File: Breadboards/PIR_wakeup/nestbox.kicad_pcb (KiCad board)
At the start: 2 copper layers, 42.8 x 27.5 mm, 13 parts, among them P1 PINOUT

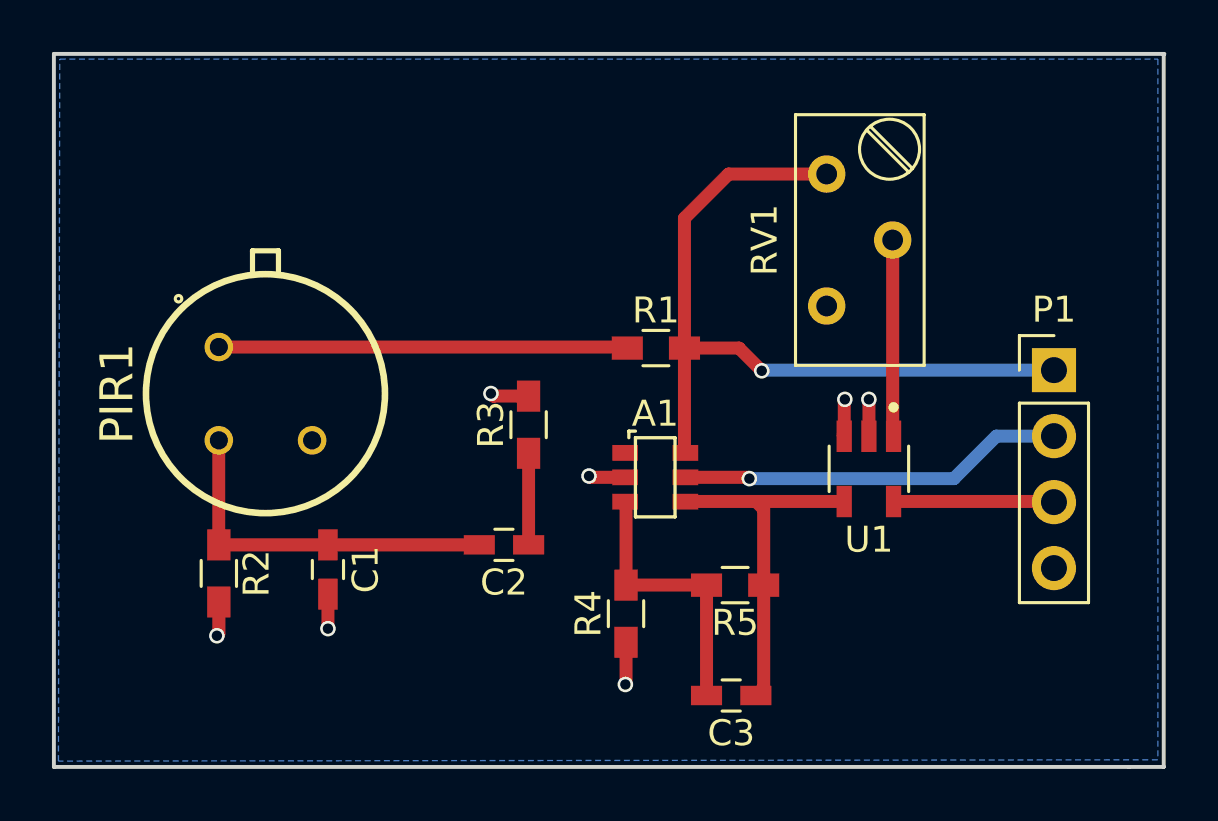
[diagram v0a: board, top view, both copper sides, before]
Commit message: Updated version of PCB
-Added component values on silk
- Added output pin connections on silk
- Cleaned silk and made it consistent trough all components
- Changed vias width to comply to manufacturer specifications
- Added missing trace
- Added decoupling capacitor on power input
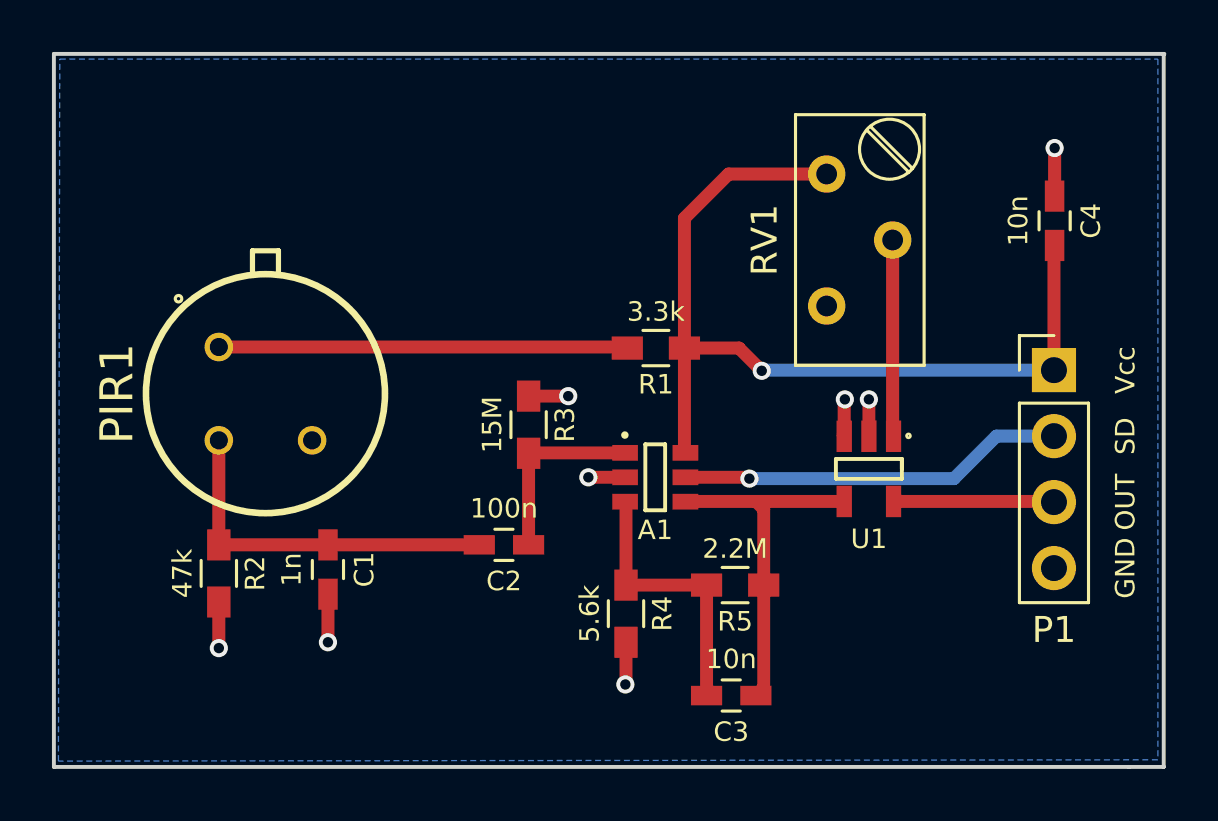
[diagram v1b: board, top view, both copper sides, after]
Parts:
- added C4: 10n, Capacitors_SMD:C_0603_HandSoldering, F.Cu at (152.3, 100.0)
- A1: footprint LTC:LTC2063 -> LTC2063
- PIR1: footprint IRA:IRA-S210ST01 -> IRA-S210ST01
- R1: value (none) -> 3.3k
- R4: value (none) -> 5.6k
- U1: footprint MAX:MAX9061 -> MAX9061
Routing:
- net Net-(A1-Pad6): track 29.8 -> 34.6 mm
- net Net-(A1-Pad1): track 3.53 -> 7.25 mm
- net GND: track 10.1 -> 13.0 mm, vias 7 -> 8
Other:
- net class Default: via_dia 0.6 -> 0.7
- rule trace_min: 0.2 -> 0.4
- rule via_min_size: 0.4 -> 0.7
- board text added: "GND"
- board text added: "OUT"
- board text added: "SD"
- board text added: "Vcc"

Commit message: Added mounting holes
Added mounting holes for M3 bolts
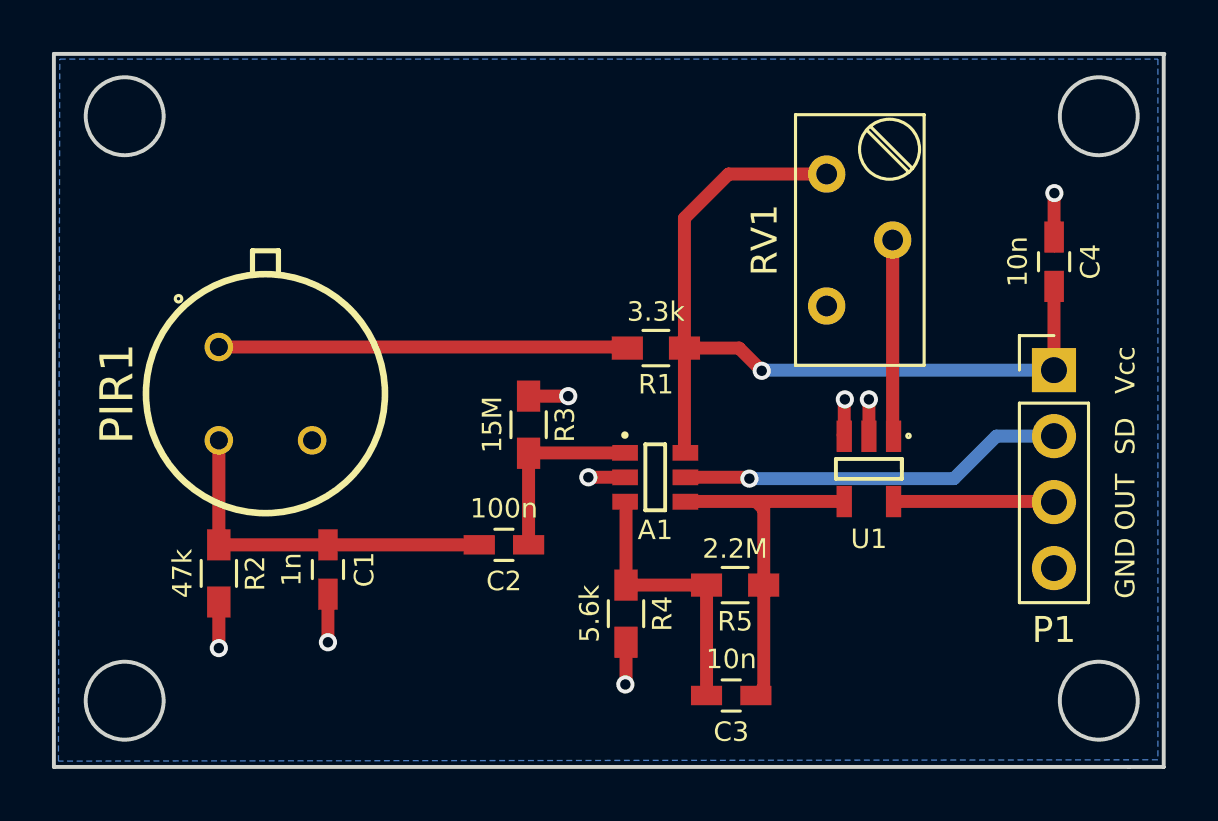
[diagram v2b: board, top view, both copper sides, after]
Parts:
- P1: value PINOUT -> (none)
- moved C4 1.58 mm to (152.3, 101.6)
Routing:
- net Net-(A1-Pad6): track 34.6 -> 33.1 mm
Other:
- outline, holes or cut-outs redrawn
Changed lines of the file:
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@@
     (area 113.699999 93.524999 156.600001 121.125001)
     (thickness 1.6)
-    (drawings 9)
-    (tracks 61)
+    (drawings 13)
+    (tracks 63)
     (zones 0)
     (modules 14)
@@
       (drillshape 0)
       (scaleselection 1)
-      (outputdirectory Nestbox_PIR/))
+      (outputdirectory gerber/))
   )
   (net 0 "")
@@
       (effects (font (size 1 1) (thickness 0.15)))
     )
-    (fp_text value PINOUT (at 0 11.85) (layer F.Fab)
+    (fp_text value "" (at -4.275 9.725) (layer F.Fab)
       (effects (font (size 1 1) (thickness 0.15)))
     )
@@
   )
   (module Capacitors_SMD:C_0603_HandSoldering (layer F.Cu)
-    (at 152.3 100.025 90)
+    (at 152.28 101.6 90)
     (descr "Capacitor SMD 0603, hand soldering")
     (tags "capacitor 0603")
@@
     )
   )
+  (gr_circle (center 154 118.5) (end 152.5 118.5) (layer Edge.Cuts) (width 0.15))
+  (gr_circle (center 154 96) (end 152.5 96) (layer Edge.Cuts) (width 0.15))
+  (gr_circle (center 116.5 118.5) (end 118 118.5) (layer Edge.Cuts) (width 0.15))
+  (gr_circle (center 116.5 96) (end 118 96) (layer Edge.Cuts) (width 0.15))
   (gr_text GND (at 155.025 113.395 90) (layer F.SilkS)
     (effects (font (size 0.75 0.75) (thickness 0.15)))
@@
   (segment (start 132.0648 108.9602) (end 132.05 108.975) (width 0.5) (layer F.Cu) (net 1))
   (segment (start 132.05 112.5) (end 132.05 108.975) (width 0.5) (layer F.Cu) (net 1))
+  (segment (start 152.28 100.65) (end 152.28 98.97) (width 0.5) (layer F.Cu) (net 2))
+  (via (at 152.29 98.96) (size 0.7) (drill 0.4) (layers F.Cu B.Cu) (net 2))
+  (segment (start 152.28 98.97) (end 152.29 98.96) (width 0.5) (layer F.Cu) (net 2))
   (segment (start 120.125 114.7) (end 120.125 116.475) (width 0.5) (layer F.Cu) (net 2))
   (via (at 120.125 116.475) (size 0.7) (drill 0.4) (layers F.Cu B.Cu) (net 2))
@@
   (segment (start 135.76422 109.9) (end 134.35 109.9) (width 0.5) (layer F.Cu) (net 2))
   (via (at 134.35 109.9) (size 0.7) (drill 0.4) (layers F.Cu B.Cu) (net 2))
-  (segment (start 152.3 99.075) (end 152.3 97.225) (width 0.5) (layer F.Cu) (net 2))
-  (via (at 152.3 97.225) (size 0.7) (drill 0.4) (layers F.Cu B.Cu) (net 2))
   (segment (start 145.15 108.32) (end 145.15 106.9) (width 0.5) (layer F.Cu) (net 2))
   (via (at 145.15 106.9) (size 0.7) (drill 0.4) (layers F.Cu B.Cu) (net 2))
@@
   (via (at 135.775 117.875) (size 0.7) (drill 0.4) (layers F.Cu B.Cu) (net 2))
   (segment (start 135.8 117.85) (end 135.775 117.875) (width 0.5) (layer F.Cu) (net 2))
+  (segment (start 152.275 101) (end 152.3 100.975) (width 0.5) (layer F.Cu) (net 2))
   (segment (start 135.8 114.05) (end 135.8 110.87558) (width 0.5) (layer F.Cu) (net 3))
   (segment (start 135.8 110.87558) (end 135.76422 110.8398) (width 0.5) (layer F.Cu) (net 3))
@@
   (segment (start 148.425 109.95) (end 140.55 109.95) (width 0.5) (layer B.Cu) (net 5))
   (segment (start 150.06 108.315) (end 148.425 109.95) (width 0.5) (layer B.Cu) (net 5))
-  (segment (start 152.275 105.775) (end 152.275 101) (width 0.5) (layer F.Cu) (net 6))
-  (segment (start 152.275 101) (end 152.3 100.975) (width 0.5) (layer F.Cu) (net 6))
+  (segment (start 152.275 105.775) (end 152.275 102.555) (width 0.5) (layer F.Cu) (net 6))
+  (segment (start 152.275 102.555) (end 152.28 102.55) (width 0.5) (layer F.Cu) (net 6))
   (segment (start 143.525 98.225) (end 139.75 98.225) (width 0.5) (layer F.Cu) (net 6))
   (segment (start 138.05 99.925) (end 138.05 104.925) (width 0.5) (layer F.Cu) (net 6))

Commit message: Mounting holes update
Change mounting holes to 5mm diameter
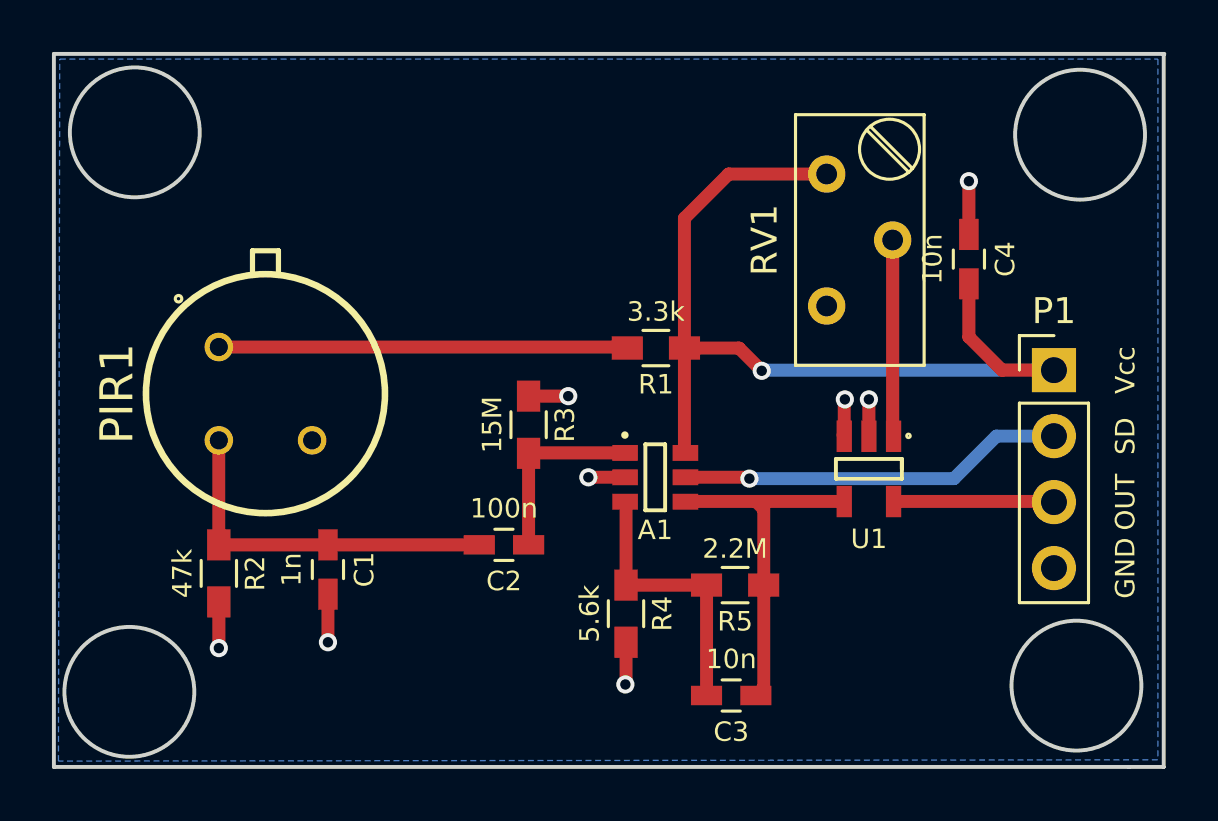
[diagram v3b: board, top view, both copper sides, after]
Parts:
- RV1: value POT -> (none)
- moved C4 3.28 mm to (149.0, 101.5)
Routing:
- net Net-(A1-Pad6): track 33.1 -> 35.7 mm
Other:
- outline, holes or cut-outs redrawn
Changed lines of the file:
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@@
     (thickness 1.6)
     (drawings 13)
-    (tracks 63)
+    (tracks 62)
     (zones 0)
     (modules 14)
@@
     (descr "Through hole straight pin header, 1x04, 2.54mm pitch, single row")
     (tags "Through hole pin header THT 1x04 2.54mm single row")
-    (fp_text reference P1 (at 0 10) (layer F.SilkS)
+    (fp_text reference P1 (at 0 -2.275) (layer F.SilkS)
       (effects (font (size 1 1) (thickness 0.15)))
     )
@@
       (effects (font (size 1 1) (thickness 0.15)))
     )
-    (fp_text value POT (at -2.54 4.94 90) (layer F.Fab)
+    (fp_text value "" (at -2.54 4.94 90) (layer F.Fab)
       (effects (font (size 1 1) (thickness 0.15)))
     )
@@
   )
   (module Capacitors_SMD:C_0603_HandSoldering (layer F.Cu)
-    (at 152.28 101.6 90)
+    (at 149 101.5 90)
     (descr "Capacitor SMD 0603, hand soldering")
     (tags "capacitor 0603")
@@
     )
   )
-  (gr_circle (center 154 118.5) (end 152.5 118.5) (layer Edge.Cuts) (width 0.15))
-  (gr_circle (center 154 96) (end 152.5 96) (layer Edge.Cuts) (width 0.15))
-  (gr_circle (center 116.5 118.5) (end 118 118.5) (layer Edge.Cuts) (width 0.15))
-  (gr_circle (center 116.5 96) (end 118 96) (layer Edge.Cuts) (width 0.15))
+  (gr_circle (center 153.28 96.71) (end 155.78 96.71) (layer Edge.Cuts) (width 0.15))
+  (gr_circle (center 153.14 117.92) (end 155.64 117.92) (layer Edge.Cuts) (width 0.15))
+  (gr_circle (center 116.68 118.16) (end 119.18 118.16) (layer Edge.Cuts) (width 0.15))
+  (gr_circle (center 116.89 96.62) (end 119.39 96.62) (layer Edge.Cuts) (width 0.15))
   (gr_text GND (at 155.025 113.395 90) (layer F.SilkS)
     (effects (font (size 0.75 0.75) (thickness 0.15)))
@@
   (segment (start 132.0648 108.9602) (end 132.05 108.975) (width 0.5) (layer F.Cu) (net 1))
   (segment (start 132.05 112.5) (end 132.05 108.975) (width 0.5) (layer F.Cu) (net 1))
-  (segment (start 152.28 100.65) (end 152.28 98.97) (width 0.5) (layer F.Cu) (net 2))
-  (via (at 152.29 98.96) (size 0.7) (drill 0.4) (layers F.Cu B.Cu) (net 2))
-  (segment (start 152.28 98.97) (end 152.29 98.96) (width 0.5) (layer F.Cu) (net 2))
+  (segment (start 149 100.55) (end 149 98.5) (width 0.5) (layer F.Cu) (net 2))
+  (via (at 149 98.5) (size 0.7) (drill 0.4) (layers F.Cu B.Cu) (net 2))
   (segment (start 120.125 114.7) (end 120.125 116.475) (width 0.5) (layer F.Cu) (net 2))
   (via (at 120.125 116.475) (size 0.7) (drill 0.4) (layers F.Cu B.Cu) (net 2))
@@
   (via (at 135.775 117.875) (size 0.7) (drill 0.4) (layers F.Cu B.Cu) (net 2))
   (segment (start 135.8 117.85) (end 135.775 117.875) (width 0.5) (layer F.Cu) (net 2))
-  (segment (start 152.275 101) (end 152.3 100.975) (width 0.5) (layer F.Cu) (net 2))
   (segment (start 135.8 114.05) (end 135.8 110.87558) (width 0.5) (layer F.Cu) (net 3))
   (segment (start 135.8 110.87558) (end 135.76422 110.8398) (width 0.5) (layer F.Cu) (net 3))
@@
   (segment (start 148.425 109.95) (end 140.55 109.95) (width 0.5) (layer B.Cu) (net 5))
   (segment (start 150.06 108.315) (end 148.425 109.95) (width 0.5) (layer B.Cu) (net 5))
-  (segment (start 152.275 105.775) (end 152.275 102.555) (width 0.5) (layer F.Cu) (net 6))
-  (segment (start 152.275 102.555) (end 152.28 102.55) (width 0.5) (layer F.Cu) (net 6))
+  (segment (start 152.275 105.775) (end 150.275 105.775) (width 0.5) (layer F.Cu) (net 6))
+  (segment (start 149 104.5) (end 149 102.45) (width 0.5) (layer F.Cu) (net 6))
+  (segment (start 150.275 105.775) (end 149 104.5) (width 0.5) (layer F.Cu) (net 6))
   (segment (start 143.525 98.225) (end 139.75 98.225) (width 0.5) (layer F.Cu) (net 6))
   (segment (start 138.05 99.925) (end 138.05 104.925) (width 0.5) (layer F.Cu) (net 6))

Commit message: Rule confilct
Moved some parts around to clear bigger holes
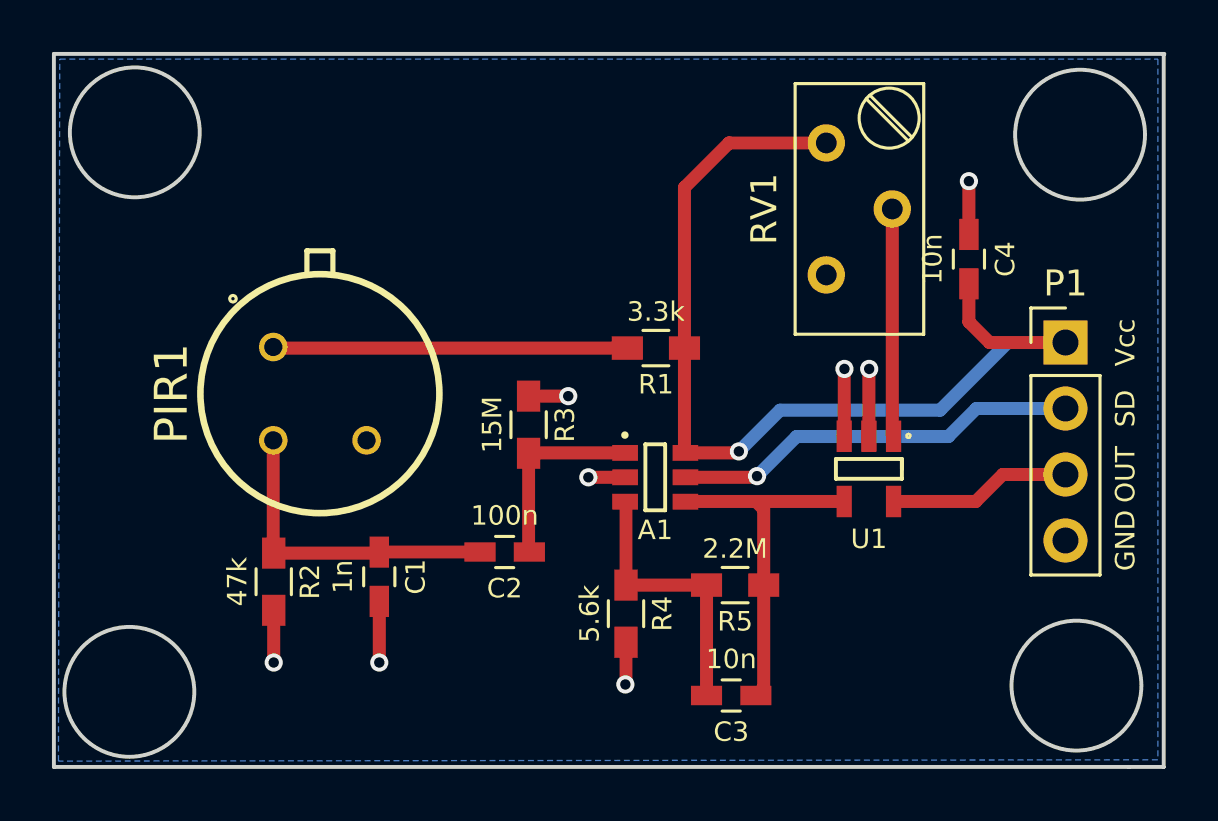
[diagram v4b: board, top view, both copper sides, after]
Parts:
- moved R2 2.14 mm to (122.2, 113.9)
- moved PIR1 2.10 mm to (124.0, 106.7)
- moved C1 2.00 mm to (126.3, 113.7)
- moved RV1 1.20 mm to (143.5, 97.0)
- moved P1 1.15 mm to (152.7, 104.7)
- moved C2 0.28 mm to (131.1, 112.8)
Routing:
- net GND: track 13.2 -> 16.2 mm
- net Net-(A1-Pad6): track 35.7 -> 38.3 mm
- net Net-(PIR1-Pad1): track 15.7 -> 13.7 mm
- net Net-(C1-Pad1): track 14.0 -> 12.3 mm
- net Net-(RV1-Pad2): track 7.57 -> 8.82 mm
- net Net-(P1-Pad3): track 6.19 -> 7.05 mm
- net Net-(A1-Pad5): track 14.9 -> 15.7 mm
